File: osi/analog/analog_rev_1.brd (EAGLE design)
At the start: 25.4 x 25.4 mm, 7 parts

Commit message: chuck
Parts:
- removed I2C_L, I2C_R: (no value), SparkFun_mod:1X05
- removed RESET: PTS635_SWITCH, _my-parts:PTS635_SWITCH
- added JP1, JP2, JP3, JP4: (no value), SparkFun:1X02
- added R3, R4: (no value), adafruit_mod:0204/7
- R1, R2: device adafruit_mod:0204V -> adafruit_mod:0204/7
- moved R2 22.9 mm to (14.0, 8.89), turned to 270 degrees
- moved R1 22.6 mm to (19.1, 8.89), turned to 270 degrees
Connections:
- removed net D1: JP8.7, R2.2
- removed net RESET: RESET.P$2
- net +3V3: now also JP1.2, JP2.2, JP3.2, JP4.2, JP8.7; no longer I2C_L.4, I2C_R.2
- net +5V: no longer I2C_L.5, I2C_R.1
- net AREF_D0: now also JP1.1, R1.1
- net D2: no longer R1.2
- net D3: now also JP2.1, R2.1
- net D5: now also JP3.1, R3.1
- net D7: now also JP4.1, R4.1
- net GND: now also R1.2, R2.2, R3.2, R4.2; no longer I2C_L.3, I2C_R.3, R1.1, R2.1, RESET.P$1
- net SCL_D4: no longer I2C_L.1, I2C_R.5
- net SDA_D6: no longer I2C_L.2, I2C_R.4
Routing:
- net +3V3: track 0.00 -> 43.8 mm
- net AREF_D0: track 0.00 -> 13.5 mm
- net D3: track 0.00 -> 12.5 mm
- net D7: track 0.00 -> 12.5 mm
- net D5: track 0.00 -> 12.5 mm
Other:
- board text added: "10k"
- board text added: "ANALOG"
- board text added: "ANALOG Rev 1 Feb 12"
- board text removed: "+5V"
- board text removed: "3V3"
- board text removed: "BRAIN"
- board text removed: "Brain Rev 1 Feb 12"
- board text removed: "RESET"
- board text removed: "SCK"
- board text removed: "SDA"

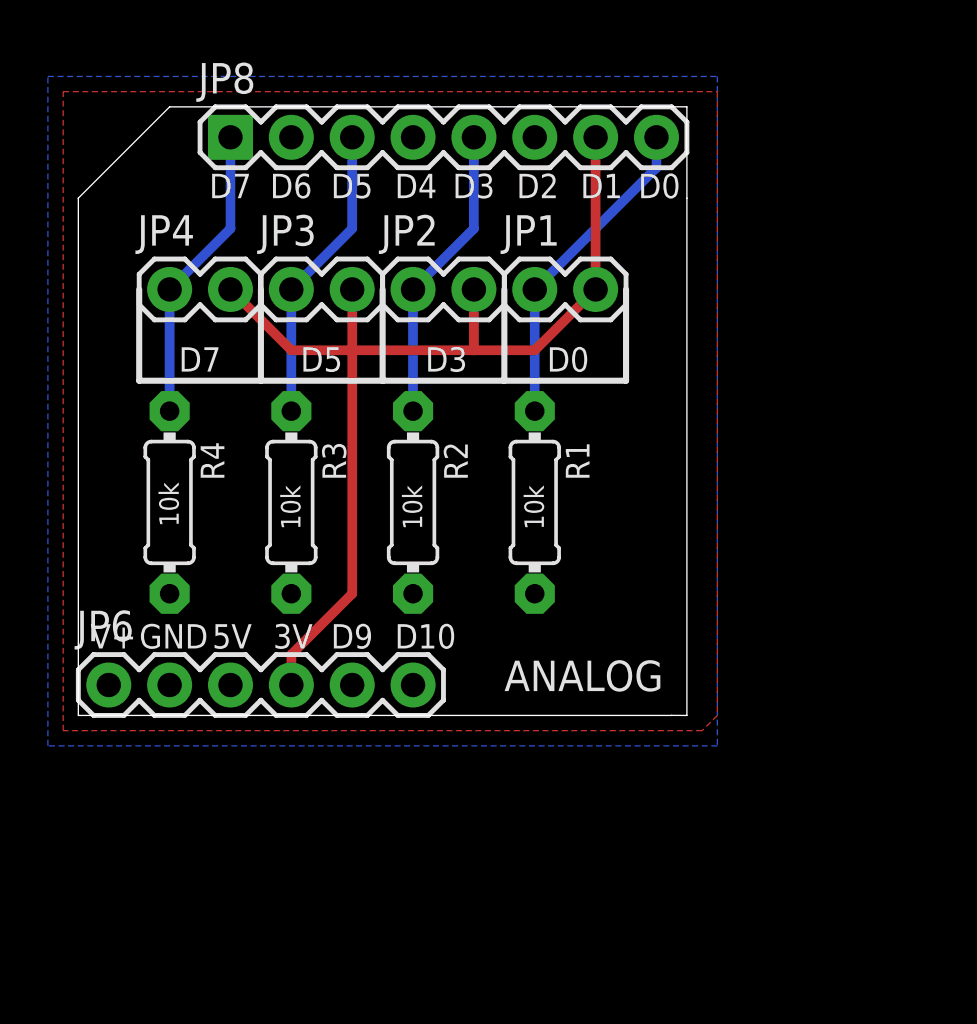
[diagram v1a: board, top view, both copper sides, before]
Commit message: D9 -> D8 for INT0
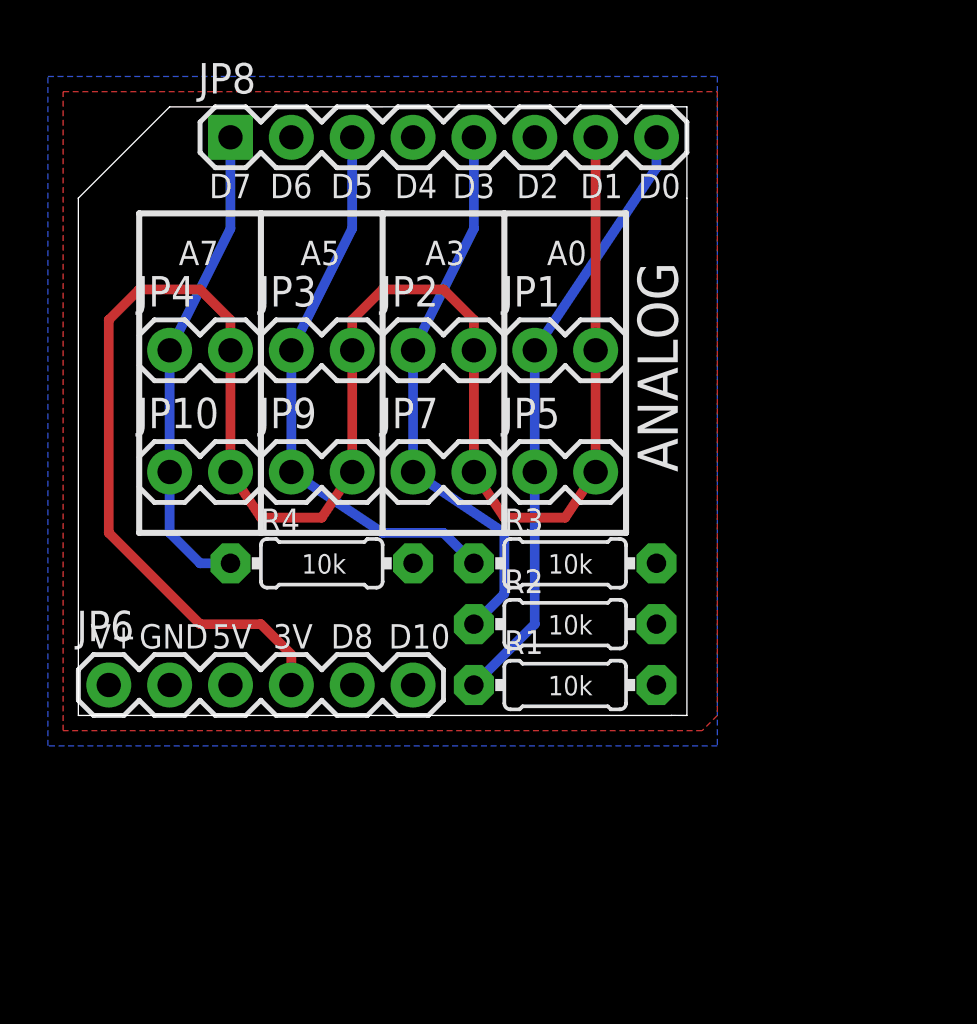
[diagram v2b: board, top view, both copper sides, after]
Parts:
- added JP10, JP5, JP7, JP9: (no value), SparkFun:1X02
- moved R3 11.7 mm to (20.3, 6.35), turned to 0 degrees
- moved R2 8.13 mm to (20.3, 3.81), turned to 0 degrees
- moved R1 7.73 mm to (20.3, 1.27), turned to 0 degrees
- moved R4 6.84 mm to (10.2, 6.35), turned to 0 degrees
- moved JP1 2.54 mm to (19.1, 15.2)
- moved JP2 2.54 mm to (14.0, 15.2)
- moved JP3 2.54 mm to (8.89, 15.2)
- moved JP4 2.54 mm to (3.81, 15.2)
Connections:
- net D9 renamed D8
- removed net +3V3: JP1.2, JP2.2, JP3.2, JP4.2, JP6.4, JP8.7
- new net D1: JP1.2, JP10.2, JP2.2, JP3.2, JP4.2, JP5.2, JP6.4, JP7.2, JP8.7, JP9.2
- net AREF_D0: now also JP5.1
- net D3: now also JP7.1
- net D5: now also JP9.1
- net D7: now also JP10.1
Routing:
- net D1: track 0.00 -> 79.4 mm
- net +3V3: track 43.8 -> 0.00 mm
- net AREF_D0: track 13.5 -> 25.5 mm
- net D5: track 12.5 -> 23.5 mm
- net D3: track 12.5 -> 23.5 mm
- net D7: track 12.5 -> 20.2 mm
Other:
- board text added: "A0"
- board text added: "A3"
- board text added: "A5"
- board text added: "A7"
- board text added: "D8"
- board text removed: "D9"
